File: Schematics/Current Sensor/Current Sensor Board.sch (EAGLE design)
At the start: 4 parts

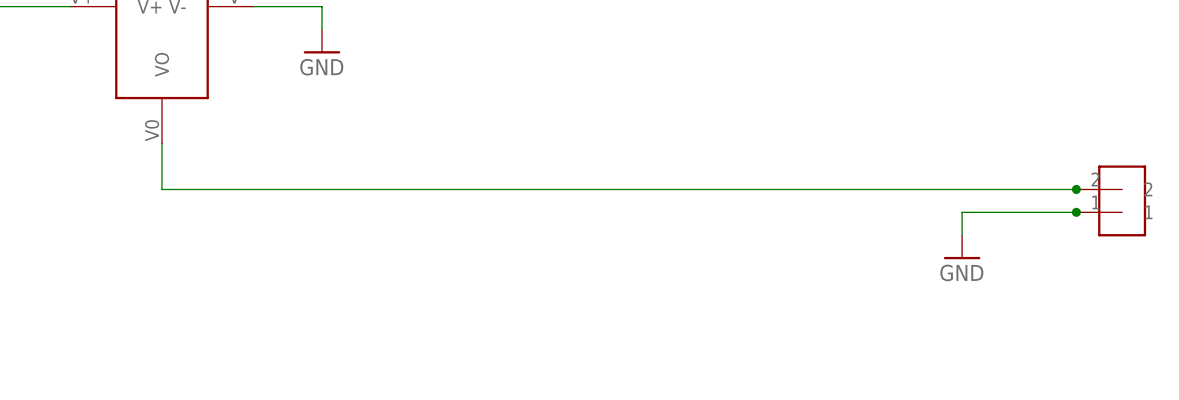
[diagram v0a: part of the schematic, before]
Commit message: added berbers for current sensor board and flowchart
flow chart is for the main control program.
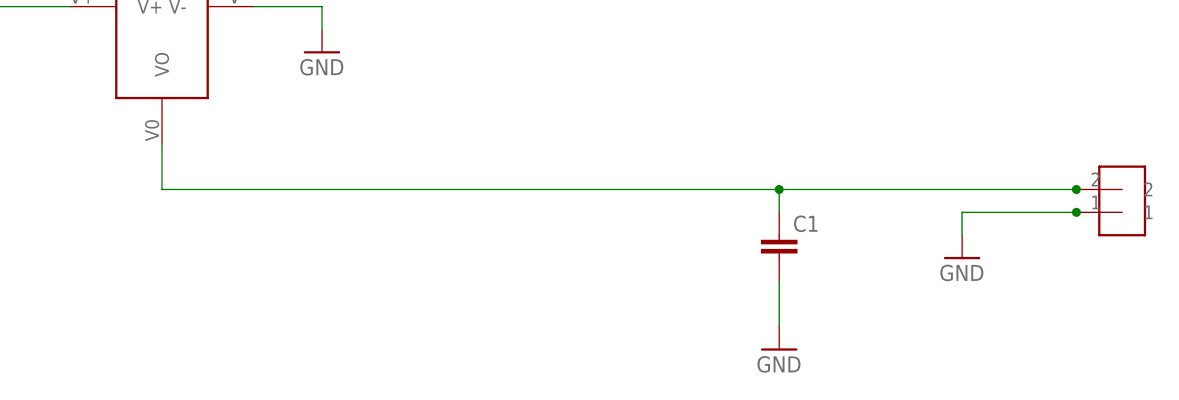
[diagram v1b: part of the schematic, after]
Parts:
- added C1: (no value), rcl:C-EU050-050X075
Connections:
- net GND: now also C1.2
- net N$3: now also C1.1
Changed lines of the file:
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@@
 <setting verticaltext="up"/>
 </settings>
-<grid distance="0.1" unitdist="inch" unit="inch" style="lines" multiple="1" display="yes" altdistance="0.01" altunitdist="inch" altunit="inch"/>
+<grid distance="0.1" unitdist="inch" unit="inch" style="lines" multiple="1" display="no" altdistance="0.01" altunitdist="inch" altunit="inch"/>
 <layers>
 <layer number="1" name="Top" color="4" fill="1" visible="no" active="no"/>
@@
 <part name="U$3" library="Headers" deviceset="1X2HEADER_100MIL" device=""/>
 <part name="IC1" library="v-reg" deviceset="78XXS" device=""/>
+<part name="C1" library="rcl" deviceset="C-EU" device="050-050X075"/>
+<part name="GND6" library="supply1" deviceset="GND" device=""/>
 </parts>
 <sheets>
@@
 <instance part="U$3" gate="G$1" x="7.62" y="185.42"/>
 <instance part="IC1" gate="1" x="66.04" y="187.96"/>
+<instance part="C1" gate="G$1" x="134.62" y="127"/>
+<instance part="GND6" gate="1" x="134.62" y="114.3"/>
 </instances>
 <busses>
@@
 <junction x="167.64" y="129.54"/>
 </segment>
+<segment>
+<pinref part="C1" gate="G$1" pin="2"/>
+<wire x1="134.62" y1="121.92" x2="134.62" y2="116.84" width="0.1524" layer="91"/>
+<pinref part="GND6" gate="1" pin="GND"/>
+</segment>
 </net>
 <net name="N$3" class="0">
@@
 <pinref part="U$1" gate="G$1" pin="VO"/>
 <wire x1="66.04" y1="137.16" x2="66.04" y2="132.08" width="0.1524" layer="91"/>
-<wire x1="66.04" y1="132.08" x2="167.64" y2="132.08" width="0.1524" layer="91"/>
+<wire x1="66.04" y1="132.08" x2="134.62" y2="132.08" width="0.1524" layer="91"/>
 <pinref part="U$2" gate="G$1" pin="2"/>
 <junction x="167.64" y="132.08"/>
+<pinref part="C1" gate="G$1" pin="1"/>
+<wire x1="134.62" y1="132.08" x2="167.64" y2="132.08" width="0.1524" layer="91"/>
+<wire x1="134.62" y1="129.54" x2="134.62" y2="132.08" width="0.1524" layer="91"/>
+<junction x="134.62" y="132.08"/>
 </segment>
 </net>
